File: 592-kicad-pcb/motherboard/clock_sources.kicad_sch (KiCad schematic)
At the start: 32 parts, among them J9 U.FL, U10 SN74LVC1G3157DBVR, U6 SMXS-04K, U7 SX3M10.000B10F20TNN, U8 74LVC1T45GW, U9 SN74LVC1G3157DBVR, Y1 NX3225GA-25.000M-STD-CRG-2, Y2 Si5351A

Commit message: finalize termination
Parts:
- added R70: 0, symbol Device:R_Small
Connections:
- net CLK_DIG_GPIO_GEN: now also R70.1; no longer R34.2, U10.3 (B1)
- new net: R34.2, R70.2, U10.3 (B1)
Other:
- note added: "might need termination to match from STM (~100 ohm out)"

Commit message: update jlcpcb part numbers
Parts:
- R70: footprint (none) -> Resistor_SMD:R_0402_1005Metric
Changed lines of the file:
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@@
 			)
 		)
-		(property "Footprint" ""
+		(property "Footprint" "Resistor_SMD:R_0402_1005Metric"
 			(at 191.77 86.36 0)
 			(effects

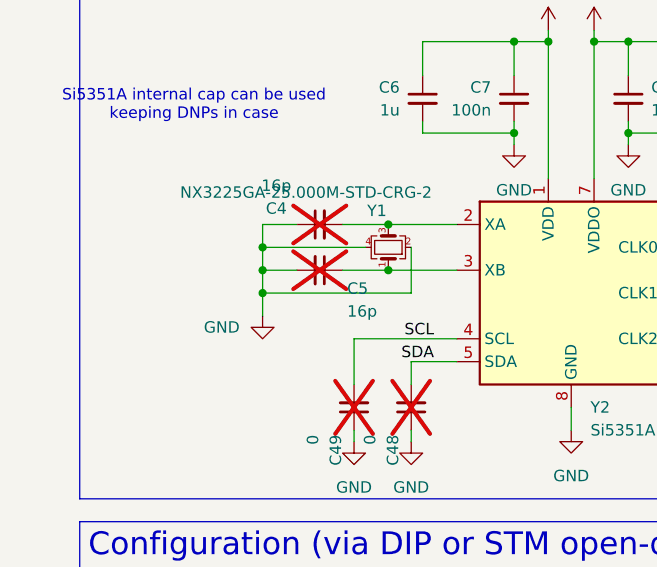
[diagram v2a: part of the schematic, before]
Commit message: further routing progess: core routing done
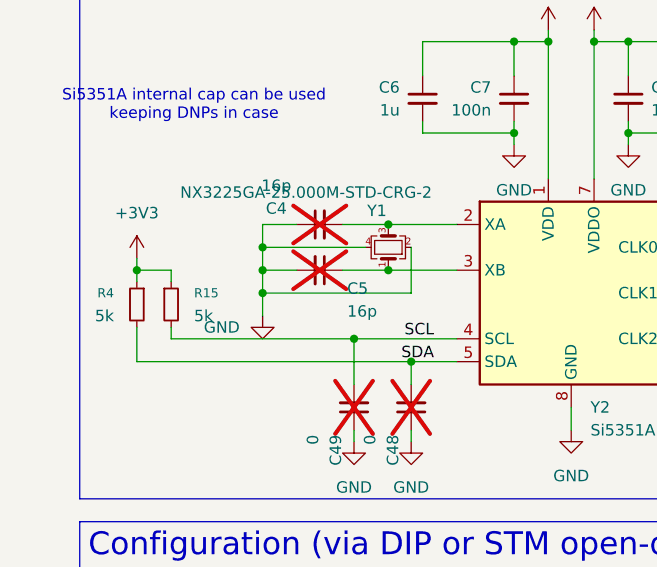
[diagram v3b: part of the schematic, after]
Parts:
- added R15, R4: 5k, Resistor_SMD:R_0402_1005Metric, symbol Device:R_Small
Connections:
- net +3V3: now also R15.1, R4.1
- net SCL: now also R15.2
- net SDA: now also R4.2
